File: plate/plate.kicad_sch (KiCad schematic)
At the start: 33 parts, among them SW0 SW_Push, SW1 SW_Push, SW10 SW_Push, SW11 SW_Push, SW12 SW_Push, SW13 SW_Push, SW14 SW_Push, SW15 SW_Push, SW2 SW_Push, SW20 SW_Push, SW21 SW_Push, SW22 SW_Push, SW23 SW_Push, SW24 SW_Push, SW25 SW_Push, SW3 SW_Push, SW30 SW_Push, SW31 SW_Push, SW32 SW_Push, SW33 SW_Push, SW34 SW_Push, SW35 SW_Push, SW4 SW_Push, SW40 SW_Push, SW41 SW_Push, SW42 SW_Push, SW43 SW_Push, SW44 SW_Push, SW45 SW_Push, SW5 SW_Push, SW50 SW_Push

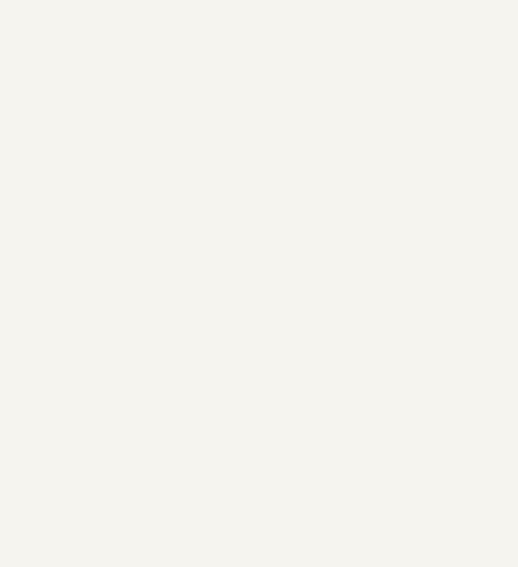
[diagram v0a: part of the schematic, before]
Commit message: update footprint of rf module
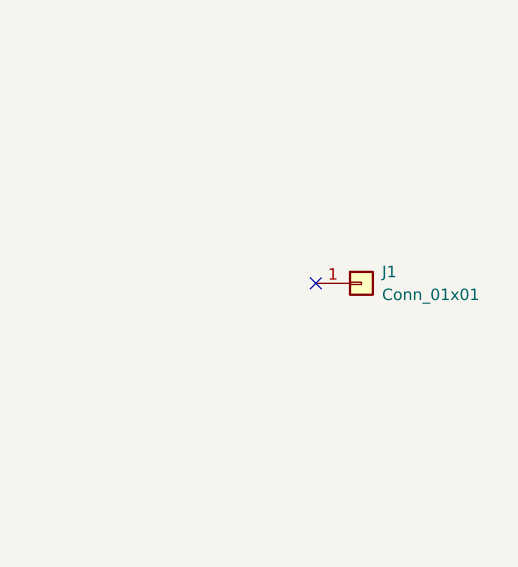
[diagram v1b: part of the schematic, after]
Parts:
- added J1: Conn_01x01, Connector_Wire:SolderWire-0.1sqmm_1x01_D0.4mm_OD1mm, symbol Connector_Generic:Conn_01x01
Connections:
- no-connect marks 0 -> 1
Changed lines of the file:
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@@
     (date "29 sep 2012")
   )
+  (no_connect (at 240.284 96.774))
   (symbol (lib_id "Mechanical:MountingHole") (at 63.5 158.75 0) (unit 1)
     (in_bom yes) (on_board yes)
@@
     )
   )
+  (symbol (lib_id "Connector_Generic:Conn_01x01") (at 245.364 96.774 0) (unit 1)
+    (in_bom yes) (on_board yes) (fields_autoplaced)
+    (property "Reference" "J1" (id 0) (at 247.65 95.5039 0)
+      (effects (font (size 1.27 1.27)) (justify left))
+    )
+    (property "Value" "Conn_01x01" (id 1) (at 247.65 98.0439 0)
+      (effects (font (size 1.27 1.27)) (justify left))
+    )
+    (property "Footprint" "Connector_Wire:SolderWire-0.1sqmm_1x01_D0.4mm_OD1mm" (id 2) (at 245.364 96.774 0)
+      (effects (font (size 1.27 1.27)) hide)
+    )
+    (property "Datasheet" "~" (id 3) (at 245.364 96.774 0)
+      (effects (font (size 1.27 1.27)) hide)
+    )
+    (pin "1")
+  )
   (sheet_instances
     (path "/" (page "1"))
@@
       (reference "H2") (unit 1) (value "MountingHole") (footprint "MountingHole:MountingHole_2.7mm_M2.5_DIN965")
     )
+    (path "/44975993-4908-46ce-9cbe-75ee0a0a699c"
+      (reference "J1") (unit 1) (value "Conn_01x01") (footprint "Connector_Wire:SolderWire-0.1sqmm_1x01_D0.4mm_OD1mm")
+    )
     (path "/00000000-0000-0000-0000-000059fc7829"
